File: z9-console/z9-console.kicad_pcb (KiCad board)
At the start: 2 copper layers, 89.5 x 55.5 mm, 130 parts, among them J10 Screw_Terminal_01x06, J2 LCD 3.2" 240x320 Conn_01x14_P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, J4 Conn_01x04_Pin, J6 ST_STDC14 - SAMTEC_FTSH-107-0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, J7 TC2070 - TAG Connect, J801 USB_C_Receptacle_USB2.0_16P, J9 JST GH, Q701 AO3400A, SW2 SW_Push, SW3 SW_Push, U10 ISM330DHCX, U11 ST_SENSOR_2, U2 TPS22919DCKR, U3 SN74LVC1G14DRLR, U5 TLV76733DRVx, U6 B0505XT-1WR3, U7 LMR14006YDDCR, U8 STM32F427V_G-I_Tx, U951 ISO1042-Q1, X2 8MHz 20pF

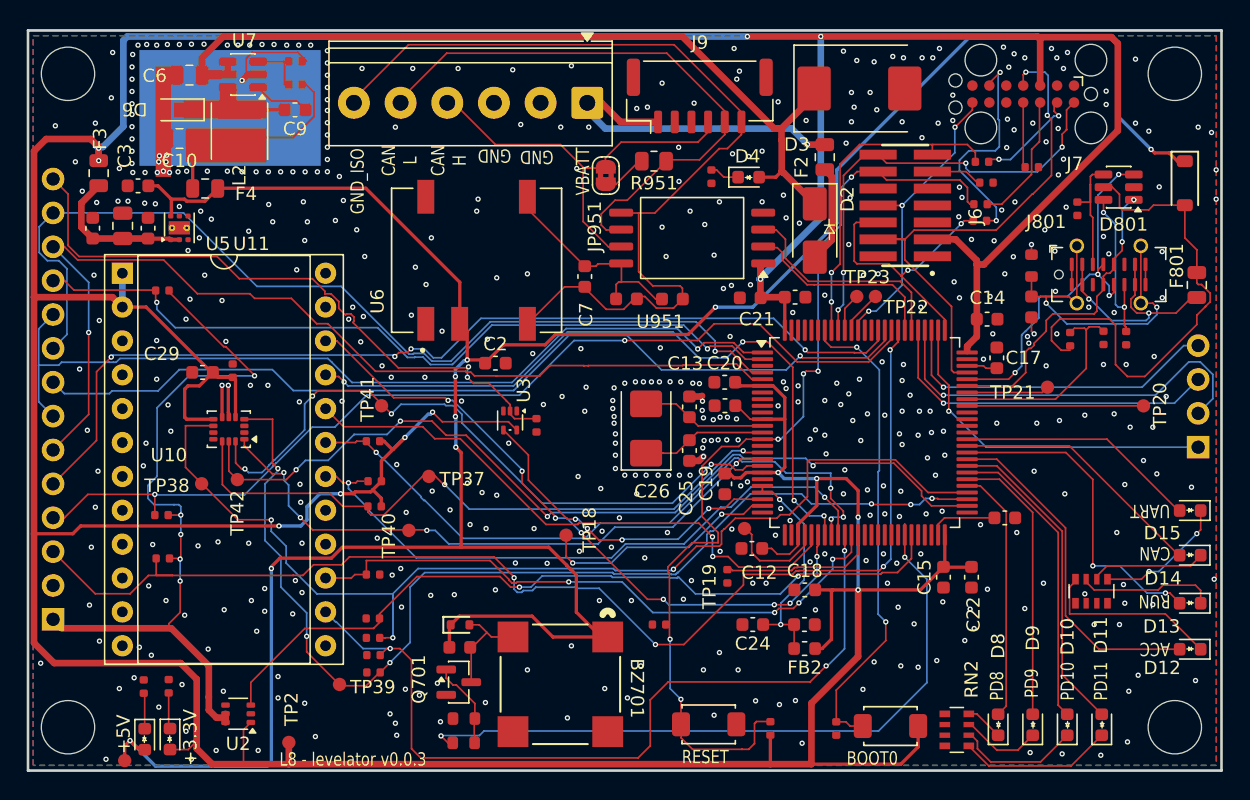
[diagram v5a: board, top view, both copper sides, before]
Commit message: fix stdc - reroute power on pcb
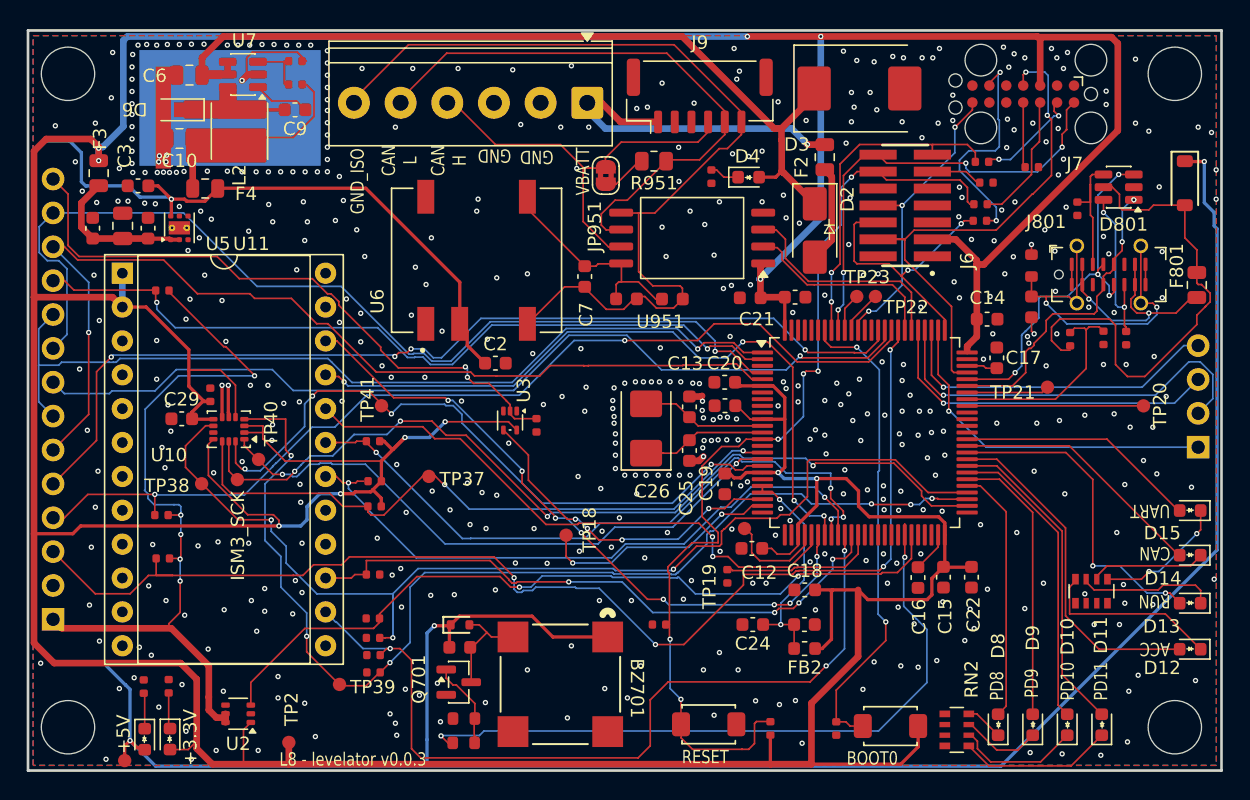
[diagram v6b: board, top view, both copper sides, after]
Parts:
- TP37: value IIS3DHHCTR_SDI -> ISM_CS
- TP38: value IIS3DHHCTR_SDI -> ISM_INT1
- TP39: value IIS3DHHCTR_SDI -> ISM_INT2
- TP40: value IIS3DHHCTR_SDI -> ISM_SDO
- TP41: value IIS3DHHCTR_SDI -> ISM_SDI
- TP42: value IIS3DHHCTR_SCK -> ISM3_SCK
- moved TP40 12.5 mm to (104.0, 104.0)
- moved C16 7.90 mm to (153.5, 112.8), turned to -90 degrees
- moved C29 3.81 mm to (98.3, 100.9)
- moved C28 2.47 mm to (100.4, 99.1)
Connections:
- U10 pad 11: unconnected-(U10-SDO_AUX-Pad11) -> +3.3V
- U10 pad 2: unconnected-(U10-SDx-Pad2) -> +3.3V
- U10 pad 3: unconnected-(U10-SCx-Pad3) -> +3.3V
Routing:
- net +5V: track 195.9 -> 247.7 mm, vias 8 -> 4
- net +3.3V: track 428.7 -> 455.3 mm, vias 13 -> 11
- net Net-(U8-VCAP_1): track 5.22 -> 3.05 mm
- net /SPI2_IRQ: track 81.4 -> 82.8 mm
- net /SPI2_IRQ2: track 84.0 -> 83.1 mm
- net Net-(J2-T_IRQ): track 47.6 -> 46.9 mm
- net Net-(J2-VCC): track 57.5 -> 58.2 mm
- net /SPI2_SDI: track 46.5 -> 46.0 mm, vias 4 -> 2
- net GND: vias 495 -> 500
